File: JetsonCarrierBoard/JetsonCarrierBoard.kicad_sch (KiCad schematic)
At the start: 0 parts

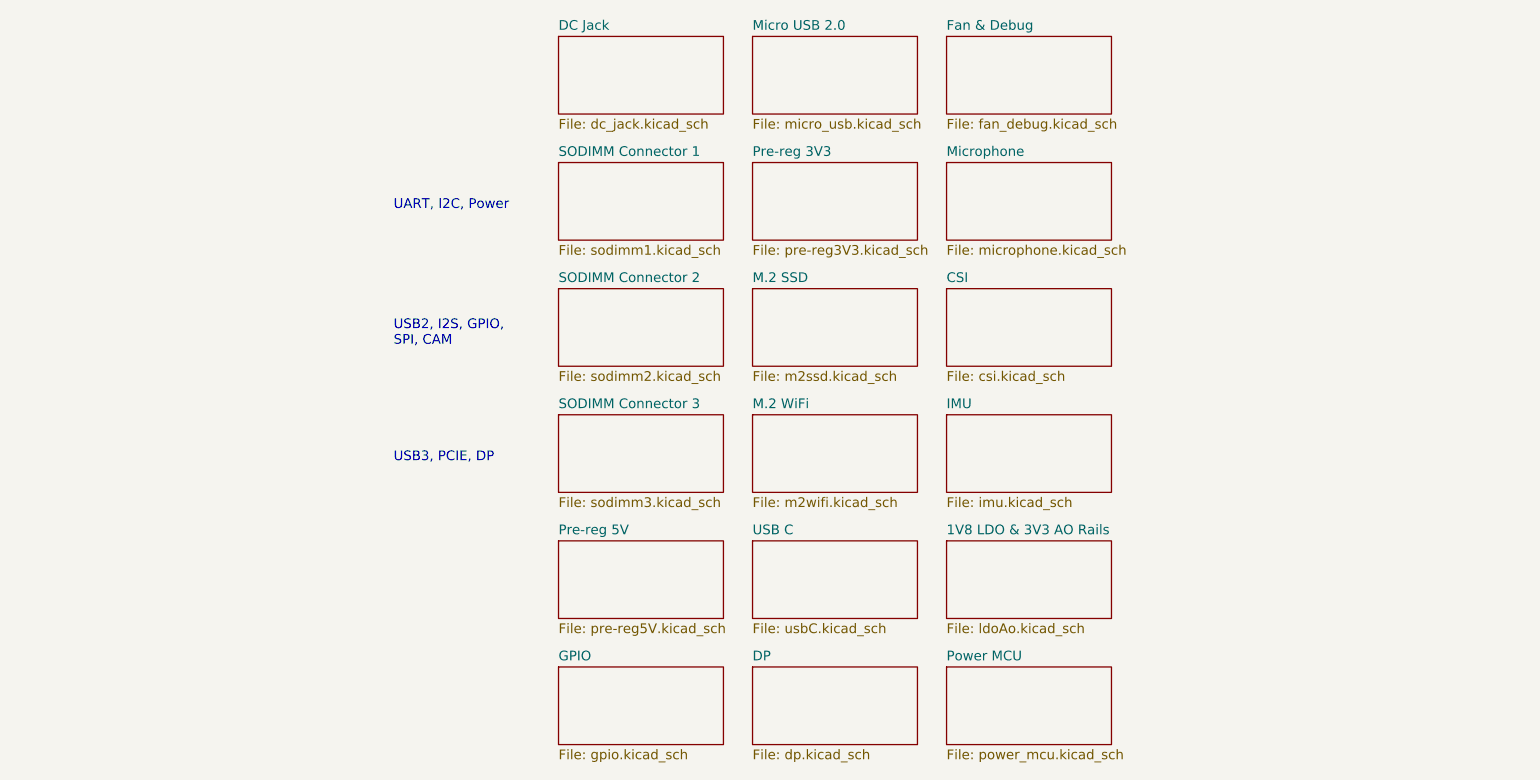
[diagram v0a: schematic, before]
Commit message: Adding more Title block info and changing main hierarchical page layout
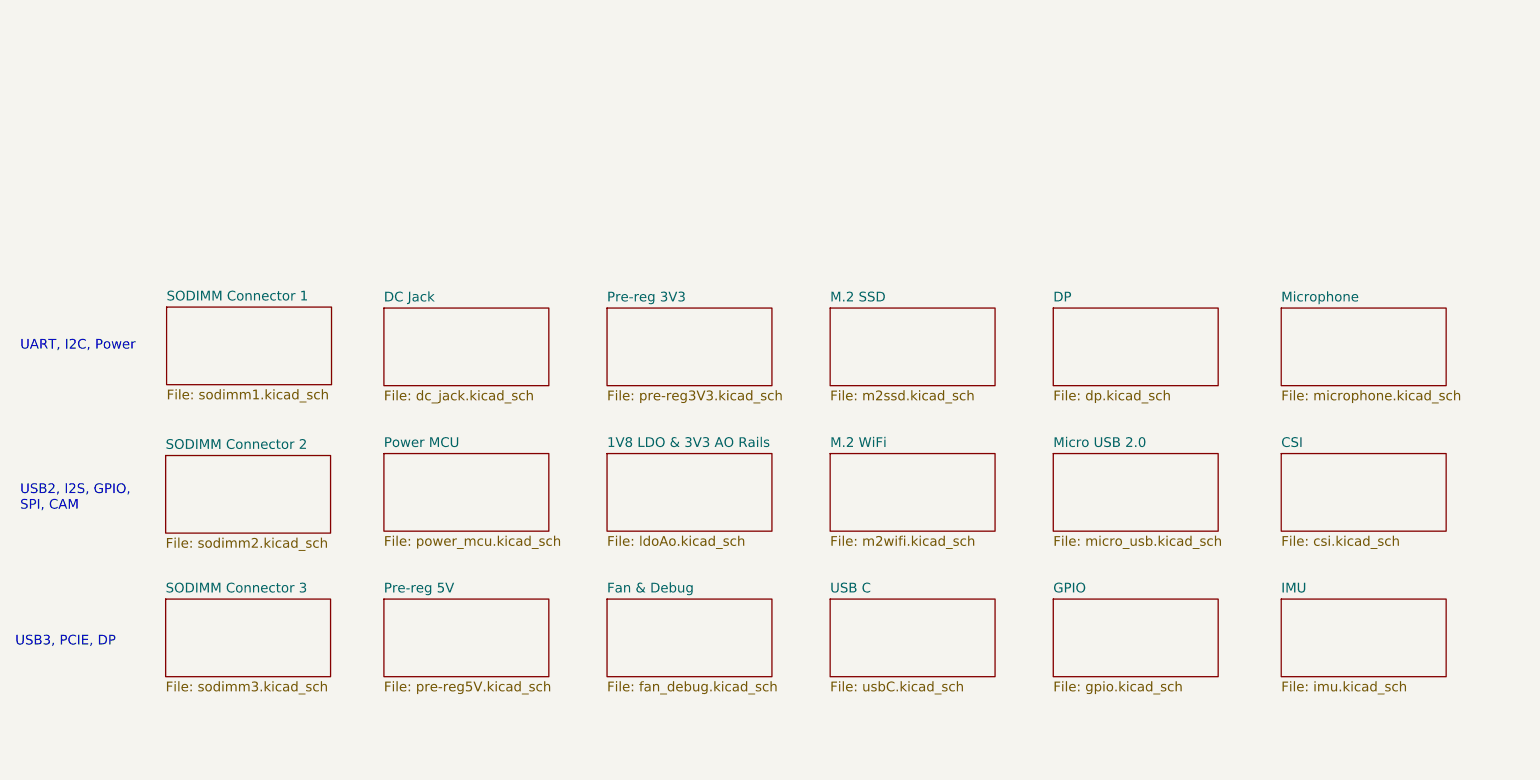
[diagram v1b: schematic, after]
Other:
- title: (none) -> Drone Jetson Carrier Board

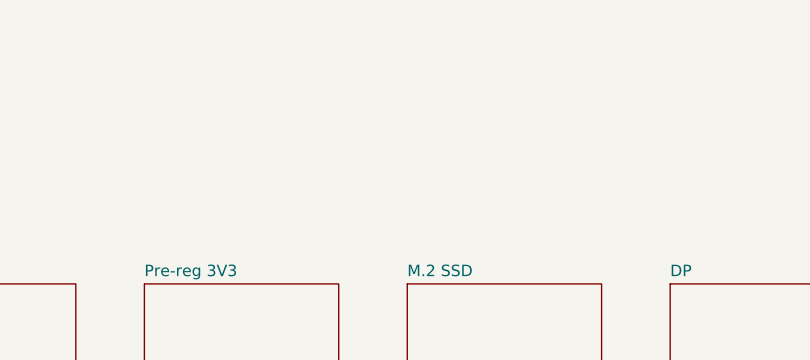
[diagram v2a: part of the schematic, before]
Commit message: Improvement list, fixes, and readability improvements
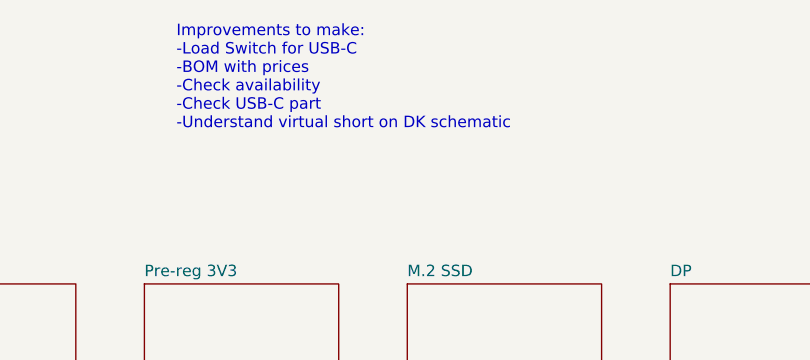
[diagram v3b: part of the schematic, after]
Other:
- note added: "Improvements to make: -Load Switch for USB-C -BOM with prices -Check availability -Check USB-C part -Understand virtual short on DK schematic"

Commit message: A ton
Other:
- note added: "Improvements to make: -Load Switch for USB-C -BOM with prices -Check availability -Check USB-C part"
- note removed: "Improvements to make: -Load Switch for USB-C -BOM with prices -Check availability -Check USB-C part -Understand virtual short on DK schematic"

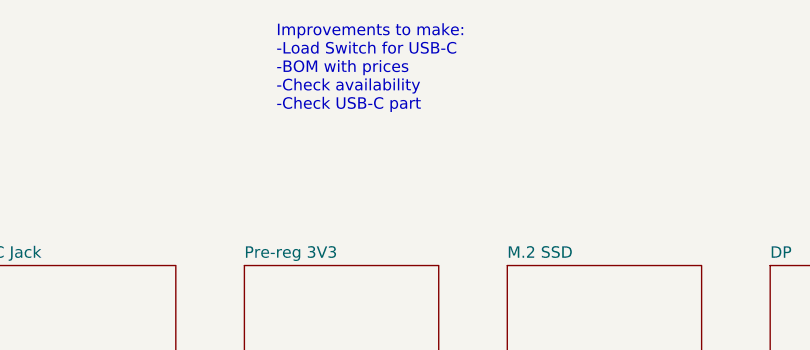
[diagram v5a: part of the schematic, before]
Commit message: Organize and Fix USB-C Part
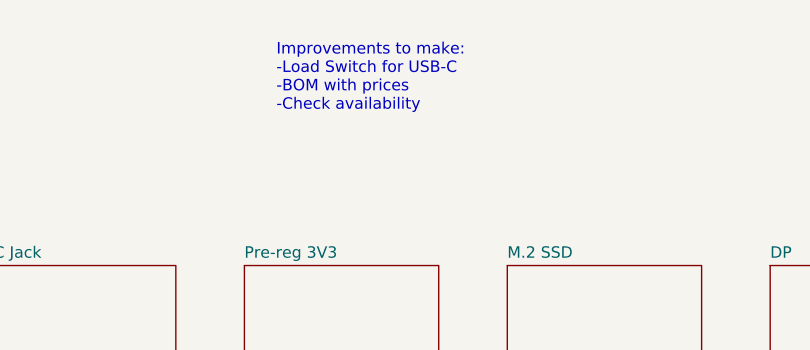
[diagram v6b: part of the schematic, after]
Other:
- note added: "Improvements to make: -Load Switch for USB-C -BOM with prices -Check availability"
- note removed: "Improvements to make: -Load Switch for USB-C -BOM with prices -Check availability -Check USB-C part"
